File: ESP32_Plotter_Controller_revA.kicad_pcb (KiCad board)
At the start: 2 copper layers, 99.1 x 55.4 mm, 40 parts, among them J1 ARM JTAG 10pin, J10 Pen Lift, J11 Vselect, J12 X Motor, J13 Y Motor, J14 Neo Pixel LEDs, J15 Pen Direction, J16 Aux Port (I2C), J2 Power, J3 5V Aux, J4 Vin Aux, J5 Limit Switches, J6 Aux Port (SPI), J7 X Limit, J8 Micro_SD_Card, J9 Y Limit, U1 ESP-DEVKITC, U2 TMC2130, U3 TMC2130, U4 XL1509

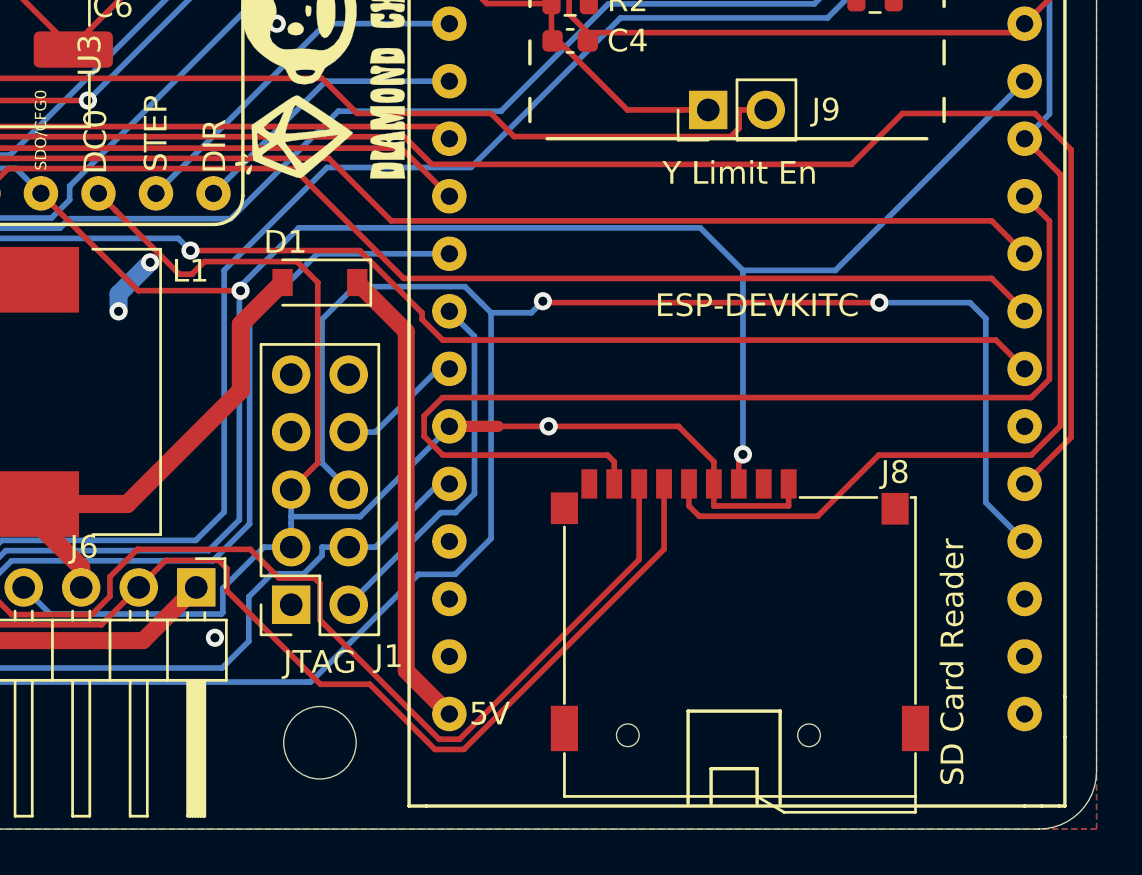
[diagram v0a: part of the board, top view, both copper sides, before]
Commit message: Fix sdcard footprint
Fix mirrored pinout on SD Card footprint.
Also grounded shield in schematic and disconnected the sd insert sense pin from gnd.
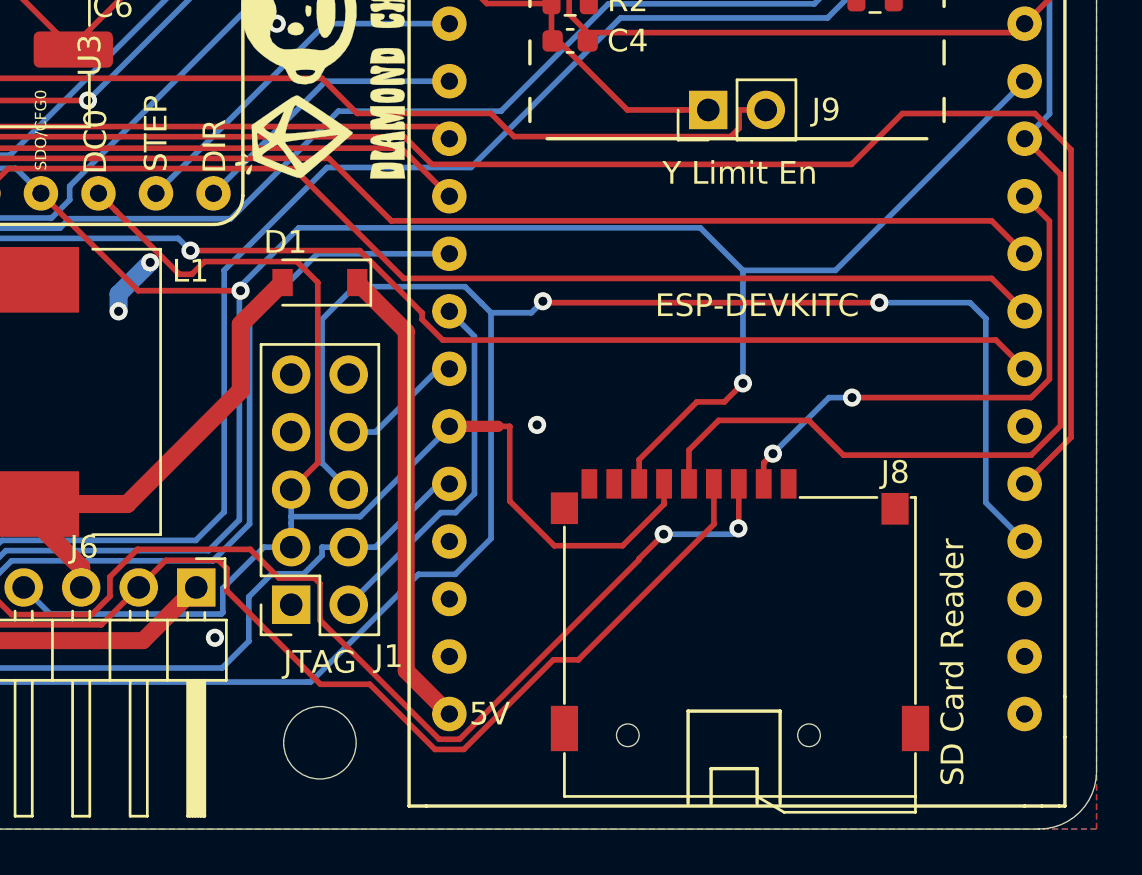
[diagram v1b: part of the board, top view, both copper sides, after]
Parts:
- J8: value Micro_SD_Card -> Micro_SD_Card_TF-01A
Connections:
- J8 pad 10: (no net) -> GND
- J8 pad 11: (no net) -> GND
- J8 pad 12: (no net) -> GND
- J8 pad 13: (no net) -> GND
- J8 pad 9: GND -> Net-(J8-Pad9)
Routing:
- net /CS_SD: track 47.5 -> 23.6 mm, vias 0 -> 2
- net GND: track 306.9 -> 303.6 mm
- net /MOSI: track 171.4 -> 174.5 mm, vias 1 -> 3
- net /MISO: track 110.4 -> 113.0 mm
- net +3V3: track 189.0 -> 190.1 mm
